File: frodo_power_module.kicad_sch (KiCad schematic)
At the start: 39 parts, among them J1 Keystone 1098, J10 SWD Header, J2 Molex MicroFit 2x2, J3 Molex MicroFit 2x2, J4 Molex MicroFit 2x2, J5 Molex MicroFit 2x2, J6 Molex MicroFit 2x2, J7 JST-GH, J8 JST-GH, J9 JST-GH, SW1 EVQ-PUC02K, SW2 EVQ-PUC02K, U1 STM32F042F6Px, U2 L7805, U3 AZ1117I-3.3, U4 BQ25171-Q1, U5 BQ29200, U6 MCP2562-E-SN, Y1 8MHz

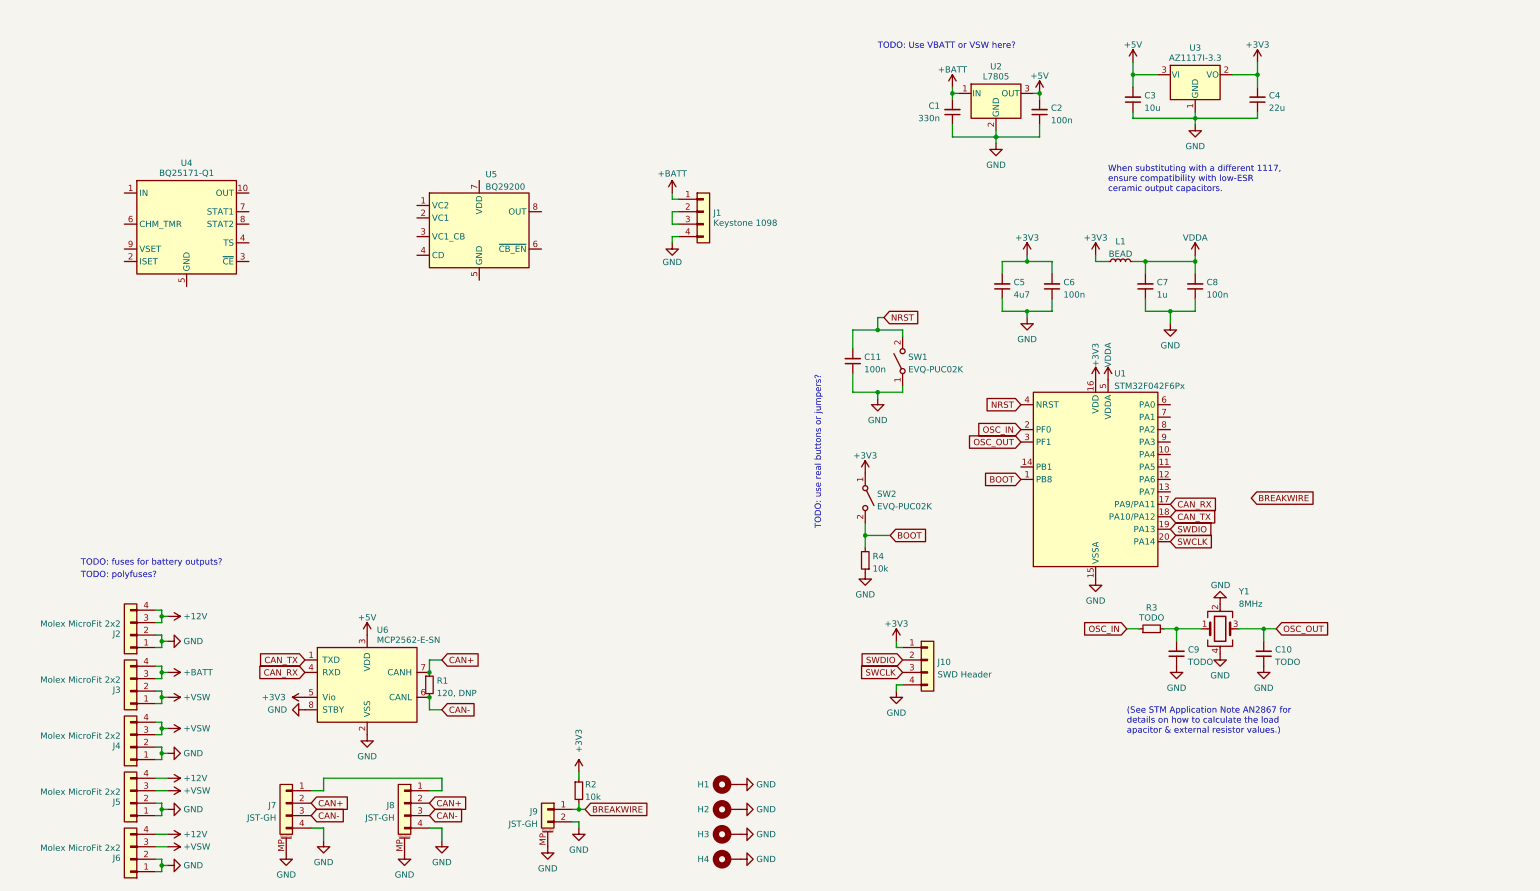
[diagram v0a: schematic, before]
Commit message: Add battery IC circuits
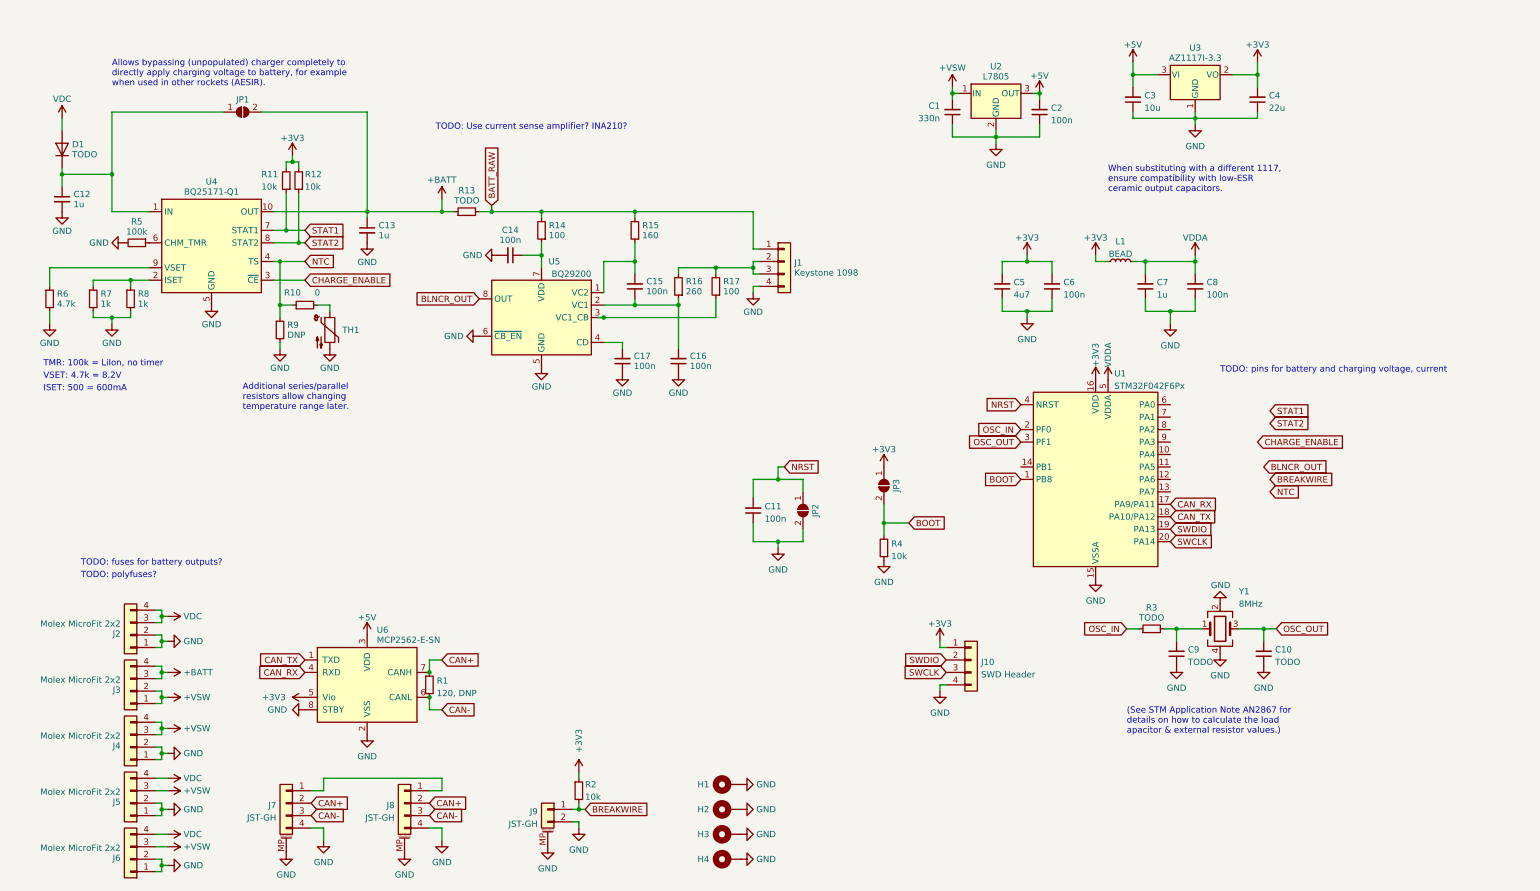
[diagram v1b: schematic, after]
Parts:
- removed SW1, SW2: EVQ-PUC02K, Button_Switch_SMD:Panasonic_EVQPUL_EVQPUC, symbol Switch:SW_SPST
- added C12, C13: 1u, Capacitor_SMD:C_0805_2012Metric, symbol Device:C_Small
- added C14, C15, C16, C17: 100n, Capacitor_SMD:C_0603_1608Metric, symbol Device:C_Small
- added D1: TODO, symbol Device:D
- added JP1, JP2, JP3: SolderJumper_2_Open, Jumper:SolderJumper-2_P1.3mm_Open_RoundedPad1.0x1.5mm, symbol Jumper:SolderJumper_2_Open
- added R10: 0, Resistor_SMD:R_0603_1608Metric, symbol Device:R_Small
- added R11, R12: 10k, Resistor_SMD:R_0603_1608Metric, symbol Device:R_Small
- added R13: TODO, Resistor_SMD:R_2512_6332Metric, symbol Device:R_Small
- added R14, R17: 100, Resistor_SMD:R_0603_1608Metric, symbol Device:R_Small
- added R15: 160, Resistor_SMD:R_0603_1608Metric, symbol Device:R_Small
- added R16: 260, Resistor_SMD:R_0603_1608Metric, symbol Device:R_Small
- added R5: 100k, Resistor_SMD:R_0603_1608Metric, symbol Device:R_Small
- added R6: 4.7k, Resistor_SMD:R_0603_1608Metric, symbol Device:R_Small
- added R7, R8: 1k, Resistor_SMD:R_0603_1608Metric, symbol Device:R_Small
- added R9: DNP, Resistor_SMD:R_0603_1608Metric, symbol Device:R_Small
- added TH1: NCU18XH103F6SRB, Resistor_SMD:R_0603_1608Metric, symbol Device:Thermistor_NTC
- H1, H2, H3, H4: footprint (none) -> MountingHole:MountingHole_3.2mm_M3_Pad_Via
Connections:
- net +3V3: now also JP3.1 (A), R11.2, R12.2
- net +BATT: now also U4.10 (OUT), C13.1, JP1.2 (B), R13.1; no longer C1.2, J1.1 (Pin_1), U2.1 (IN)
- net +VSW: now also C1.2, U2.1 (IN)
- net BOOT: now also JP3.2 (B)
- net GND: now also U4.11 (GND), U4.5 (GND), U5.5 (GND), U5.6 (~{CB_EN}), U5.9 (PWR_PAD), C12.2, C13.2, C14.2, C16.1, C17.1, JP2.2 (B), R5.2, R6.2, R7.2, R8.2, R9.2, TH1.2
- net NRST: now also JP2.1 (A)
- net at U4.1 (IN): now also C12.1, D1.1 (K), JP1.1 (A)
- net at U4.2 (ISET): now also R7.1, R8.1
- net CHARGE_ENABLE: now reaches U4.3 (~{CE})
- net NTC: now reaches U4.4 (TS)
- net NTC: now also R10.1, R9.1
- net at U4.6 (CHM_TMR): now also R5.1
- net STAT1: now reaches U4.7 (STAT1)
- net STAT1: now also R11.1
- net STAT2: now reaches U4.8 (STAT2)
- net STAT2: now also R12.1
- net at U4.9 (VSET): now also R6.1
- net at J1.2 (Pin_2), J1.3 (Pin_3): now also R16.2, R17.2
- net at U5.1 (VC2): now also C15.2, R15.1
- net at U5.2 (VC1): now also C15.1, C16.2, R16.1
- net at U5.3 (VC1_CB): now also R17.1
- net at U5.4 (CD): now also C17.2
- net at U5.7 (VDD): now also C14.1, R14.1
- net BLNCR_OUT: now reaches U5.8 (OUT)
- net +12V renamed VDC
- net VDC: now also D1.2 (A)
- new net: R10.2, TH1.1
- new net BATT_RAW: J1.1 (Pin_1), R13.2, R14.2, R15.2
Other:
- note added: "Additional series/parallel resistors allow changing temperature range later."
- note added: "Allows bypassing (unpopulated) charger completely to directly apply charging voltage to battery, for example when used in other rockets (AESIR)."
- note added: "ISET: 500 = 600mA"
- note added: "TMR: 100k = LiIon, no timer"
- note added: "TODO: Use current sense amplifier? INA210?"
- note added: "TODO: pins for battery and charging voltage, current"
- note added: "VSET: 4.7k = 8.2V"
- note removed: "TODO: Use VBATT or VSW here?"
- note removed: "TODO: use real buttons or jumpers?"
- moved on the sheet: C11, J1, J10, R4, U4, U5

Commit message: Update PCB
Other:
- note added: "TODO: diodes/(poly)fuses for battery outputs?"
- note removed: "TODO: fuses for battery outputs?"
- note removed: "TODO: polyfuses?"
- moved on the sheet: C11, J7, J8, J9, JP2, JP3, R1, R2, R4, U6

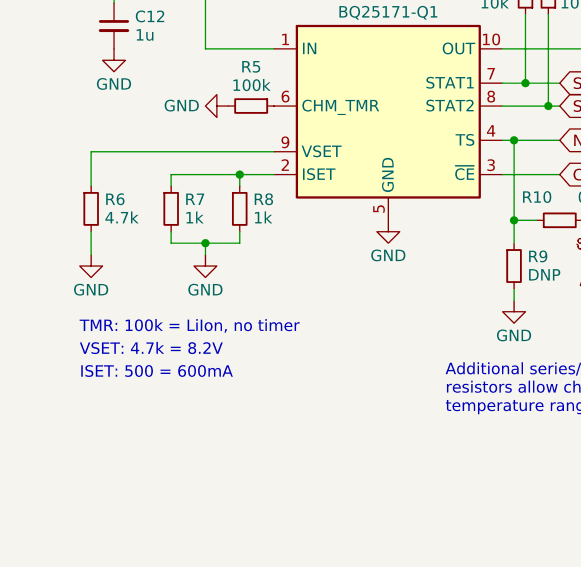
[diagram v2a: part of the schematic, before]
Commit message: Fixed VSET for charger
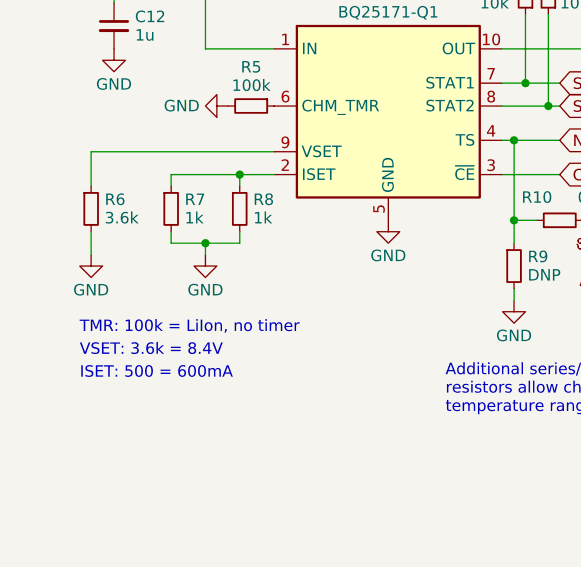
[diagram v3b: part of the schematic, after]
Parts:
- C12, C13: LCSC# (none) -> C318694; Manufacturer (none) -> Samsung Electro-Mechanics; Part# (none) -> CL21A105KBCLNNC
- C14, C15, C16, C17: LCSC# (none) -> C1591; Manufacturer (none) -> Samsung Electro-Mechanics; Part# (none) -> CL10B104KB8NNNC
- R6: value 4.7k -> 3.6k
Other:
- note added: "VSET: 3.6k = 8.4V"
- note removed: "VSET: 4.7k = 8.2V"
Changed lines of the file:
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@@
     (effects (font (size 1.27 1.27) (color 194 0 0 1)) (justify left bottom))
   )
-  (text "VSET: 4.7k = 8.2V" (at 20.32 90.17 0)
+  (text "VSET: 3.6k = 8.4V" (at 20.32 90.17 0)
     (effects (font (size 1.27 1.27)) (justify left bottom))
   )
@@
       (effects (font (size 1.27 1.27)) hide)
     )
+    (property "LCSC#" "C318694" (at 24.13 53.34 0)
+      (effects (font (size 1.27 1.27)) hide)
+    )
+    (property "Manufacturer" "Samsung Electro-Mechanics" (at 24.13 53.34 0)
+      (effects (font (size 1.27 1.27)) hide)
+    )
+    (property "Part#" "CL21A105KBCLNNC" (at 24.13 53.34 0)
+      (effects (font (size 1.27 1.27)) hide)
+    )
     (pin "1")
     (pin "2")
@@
       (effects (font (size 1.27 1.27)) hide)
     )
+    (property "LCSC#" "C1591" (at 149.86 86.36 0)
+      (effects (font (size 1.27 1.27)) hide)
+    )
+    (property "Manufacturer" "Samsung Electro-Mechanics" (at 149.86 86.36 0)
+      (effects (font (size 1.27 1.27)) hide)
+    )
+    (property "Part#" "CL10B104KB8NNNC" (at 149.86 86.36 0)
+      (effects (font (size 1.27 1.27)) hide)
+    )
     (pin "1")
     (pin "2")
@@
       (effects (font (size 1.27 1.27)) hide)
     )
+    (property "LCSC#" "C1591" (at 140.97 71.12 0)
+      (effects (font (size 1.27 1.27)) hide)
+    )
+    (property "Manufacturer" "Samsung Electro-Mechanics" (at 140.97 71.12 0)
+      (effects (font (size 1.27 1.27)) hide)
+    )
+    (property "Part#" "CL10B104KB8NNNC" (at 140.97 71.12 0)
+      (effects (font (size 1.27 1.27)) hide)
+    )
     (pin "1")
     (pin "2")
@@
       (effects (font (size 1.27 1.27)) (justify left))
     )
-    (property "Value" "4.7k" (at 23.0886 74.684 0)
+    (property "Value" "3.6k" (at 23.0886 74.684 0)
       (effects (font (size 1.27 1.27)) (justify left))
     )
@@
       (effects (font (size 1.27 1.27)) hide)
     )
+    (property "LCSC#" "C1591" (at 115.57 64.77 0)
+      (effects (font (size 1.27 1.27)) hide)
+    )
+    (property "Manufacturer" "Samsung Electro-Mechanics" (at 115.57 64.77 0)
+      (effects (font (size 1.27 1.27)) hide)
+    )
+    (property "Part#" "CL10B104KB8NNNC" (at 115.57 64.77 0)
+      (effects (font (size 1.27 1.27)) hide)
+    )
     (pin "1")
     (pin "2")
@@
       (effects (font (size 1.27 1.27)) hide)
     )
+    (property "LCSC#" "C1591" (at 138.43 86.36 0)
+      (effects (font (size 1.27 1.27)) hide)
+    )
+    (property "Manufacturer" "Samsung Electro-Mechanics" (at 138.43 86.36 0)
+      (effects (font (size 1.27 1.27)) hide)
+    )
+    (property "Part#" "CL10B104KB8NNNC" (at 138.43 86.36 0)
+      (effects (font (size 1.27 1.27)) hide)
+    )
     (pin "1")
     (pin "2")
@@
       (effects (font (size 1.27 1.27)) hide)
     )
+    (property "LCSC#" "C318694" (at 86.36 59.69 0)
+      (effects (font (size 1.27 1.27)) hide)
+    )
+    (property "Manufacturer" "Samsung Electro-Mechanics" (at 86.36 59.69 0)
+      (effects (font (size 1.27 1.27)) hide)
+    )
+    (property "Part#" "CL21A105KBCLNNC" (at 86.36 59.69 0)
+      (effects (font (size 1.27 1.27)) hide)
+    )

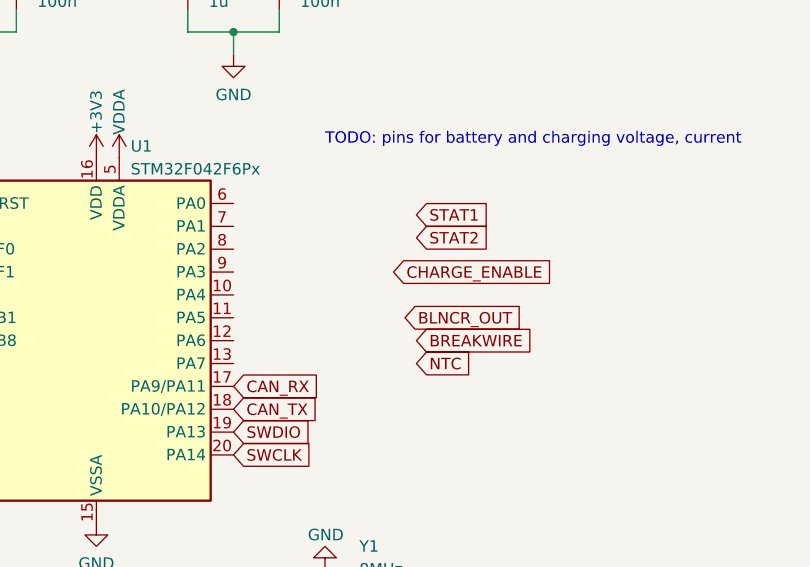
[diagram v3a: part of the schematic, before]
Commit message: created component groups on pcb
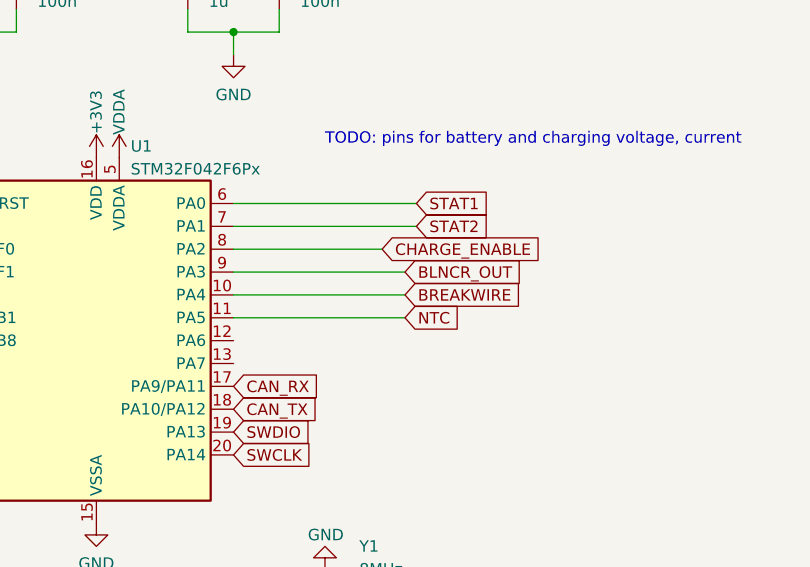
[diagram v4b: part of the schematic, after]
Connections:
- net BLNCR_OUT: now also U1.9 (PA3)
- net BREAKWIRE: now also U1.10 (PA4)
- net CHARGE_ENABLE: now also U1.8 (PA2)
- net NTC: now also U1.11 (PA5)
- net STAT1: now also U1.6 (PA0)
- net STAT2: now also U1.7 (PA1)
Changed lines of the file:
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@@
+    (stroke (width 0) (type default))
+  )
+  (wire (pts (xy 250.19 105.41) (xy 269.24 105.41))
     (stroke (width 0) (type default))
   )
@@
     (stroke (width 0) (type default))
   )
+  (wire (pts (xy 250.19 100.33) (xy 266.7 100.33))
+    (stroke (width 0) (type default))
+  )
   (wire (pts (xy 134.62 77.47) (xy 157.48 77.47))
     (stroke (width 0) (type default))
@@
     (stroke (width 0) (type default))
   )
+  (wire (pts (xy 250.19 107.95) (xy 269.24 107.95))
+    (stroke (width 0) (type default))
+  )
   (wire (pts (xy 242.57 66.04) (xy 245.11 66.04))
     (stroke (width 0) (type default))
@@
     (stroke (width 0) (type default))
   )
+  (wire (pts (xy 250.19 95.25) (xy 270.51 95.25))
+    (stroke (width 0) (type default))
+  )
   (wire (pts (xy 44.45 153.67) (xy 43.18 153.67))
     (stroke (width 0) (type default))
@@
     (stroke (width 0) (type default))
   )
+  (wire (pts (xy 250.19 102.87) (xy 269.24 102.87))
+    (stroke (width 0) (type default))
+  )
   (wire (pts (xy 111.76 181.61) (xy 109.22 181.61))
     (stroke (width 0) (type default))
@@
   )
   (wire (pts (xy 157.48 68.58) (xy 157.48 67.31))
+    (stroke (width 0) (type default))
+  )
+  (wire (pts (xy 250.19 97.79) (xy 270.51 97.79))
     (stroke (width 0) (type default))
   )
@@
     )
   )
-  (global_label "STAT2" (shape input) (at 270.51 99.06 0) (fields_autoplaced)
-    (effects (font (size 1.27 1.27)) (justify left))
-    (property "Intersheetrefs" "${INTERSHEET_REFS}" (at 278.8586 99.06 0)
-      (effects (font (size 1.27 1.27)) (justify left) hide)
-    )
-  )
-  (global_label "STAT1" (shape input) (at 270.51 96.52 0) (fields_autoplaced)
-    (effects (font (size 1.27 1.27)) (justify left))
-    (property "Intersheetrefs" "${INTERSHEET_REFS}" (at 278.8586 96.52 0)
+  (global_label "STAT2" (shape input) (at 270.51 97.79 0) (fields_autoplaced)
+    (effects (font (size 1.27 1.27)) (justify left))
+    (property "Intersheetrefs" "${INTERSHEET_REFS}" (at 278.8586 97.79 0)
+      (effects (font (size 1.27 1.27)) (justify left) hide)
+    )
+  )
+  (global_label "STAT1" (shape input) (at 270.51 95.25 0) (fields_autoplaced)
+    (effects (font (size 1.27 1.27)) (justify left))
+    (property "Intersheetrefs" "${INTERSHEET_REFS}" (at 278.8586 95.25 0)
       (effects (font (size 1.27 1.27)) (justify left) hide)
     )
@@
     )
   )
-  (global_label "NTC" (shape input) (at 270.51 113.03 0) (fields_autoplaced)
-    (effects (font (size 1.27 1.27)) (justify left))
-    (property "Intersheetrefs" "${INTERSHEET_REFS}" (at 276.9839 113.03 0)
+  (global_label "NTC" (shape input) (at 269.24 107.95 0) (fields_autoplaced)
+    (effects (font (size 1.27 1.27)) (justify left))
+    (property "Intersheetrefs" "${INTERSHEET_REFS}" (at 275.7139 107.95 0)
       (effects (font (size 1.27 1.27)) (justify left) hide)
     )
@@
     )
   )
-  (global_label "BREAKWIRE" (shape input) (at 270.51 110.49 0) (fields_autoplaced)
-    (effects (font (size 1.27 1.27)) (justify left))
-    (property "Intersheetrefs" "${INTERSHEET_REFS}" (at 283.9386 110.49 0)
+  (global_label "BREAKWIRE" (shape input) (at 269.24 105.41 0) (fields_autoplaced)
+    (effects (font (size 1.27 1.27)) (justify left))
+    (property "Intersheetrefs" "${INTERSHEET_REFS}" (at 282.6686 105.41 0)
       (effects (font (size 1.27 1.27)) (justify left) hide)
     )
@@
     )
   )
-  (global_label "CHARGE_ENABLE" (shape input) (at 267.97 102.87 0) (fields_autoplaced)
-    (effects (font (size 1.27 1.27)) (justify left))
-    (property "Intersheetrefs" "${INTERSHEET_REFS}" (at 286.2367 102.87 0)
-      (effects (font (size 1.27 1.27)) (justify left) hide)
-    )
-  )
-  (global_label "BLNCR_OUT" (shape input) (at 269.24 107.95 0) (fields_autoplaced)
-    (effects (font (size 1.27 1.27)) (justify left))
-    (property "Intersheetrefs" "${INTERSHEET_REFS}" (at 282.9106 107.95 0)
-      (effects (font (size 1.27 1.27)) (justify left) hide)
-    )
+  (global_label "CHARGE_ENABLE" (shape input) (at 266.7 100.33 0) (fields_autoplaced)
+    (effects (font (size 1.27 1.27)) (justify left))
+    (property "Intersheetrefs" "${INTERSHEET_REFS}" (at 284.9667 100.33 0)
+      (effects (font (size 1.27 1.27)) (justify left) hide)
+    )
+  )
+  (global_label "BLNCR_OUT" (shape input) (at 269.24 102.87 0) (fields_autoplaced)
+    (effects (font (size 1.27 1.27)) (justify left))
+    (property "Intersheetrefs" "${INTERSHEET_REFS}" (at 282.9106 102.87 0)
+      (effects (font (size 1.27 1.27)) (justify left) hide)
+    )
